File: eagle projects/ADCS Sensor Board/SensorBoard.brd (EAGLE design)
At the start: 91 x 91 mm, 85 parts, among them J5 HDR_10_EZFET_DEBUGGER, J6 MTI-1_8428-11B1-RK-TP, Q1 BC850SMD, Q2 IRF7507TRPBF, U1 MSP430F5529IPN, U2 LMV321, U3 ADS7841E_2K5, U4 LMV321, U5 LM20BIM7X_NOPB, U6 LMV321, Y1 32.768kHz, Y2 CSTCR4M00G15L99

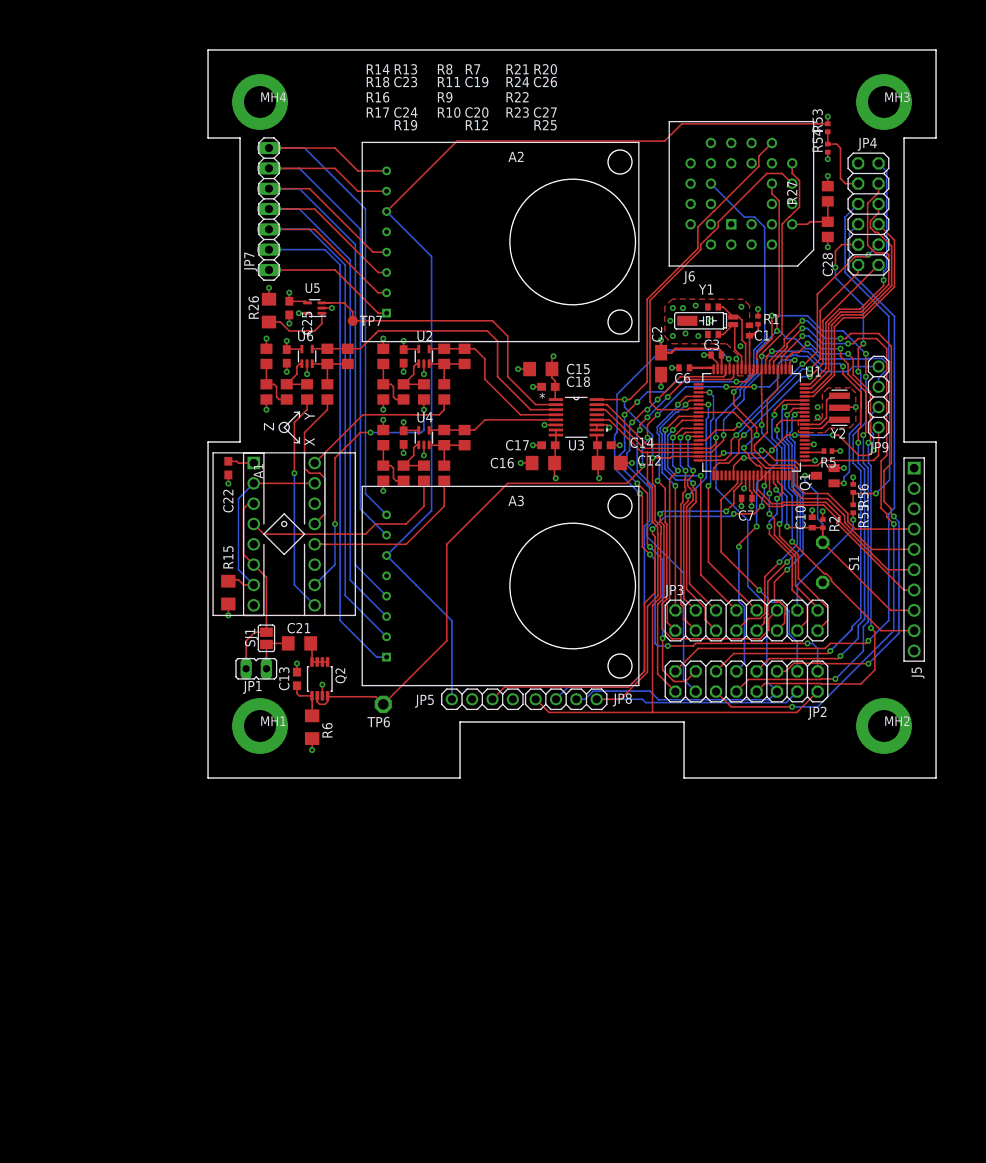
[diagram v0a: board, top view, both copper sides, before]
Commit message: Added copper pours to top and bottom. Fixed silksreens, smoothed traces
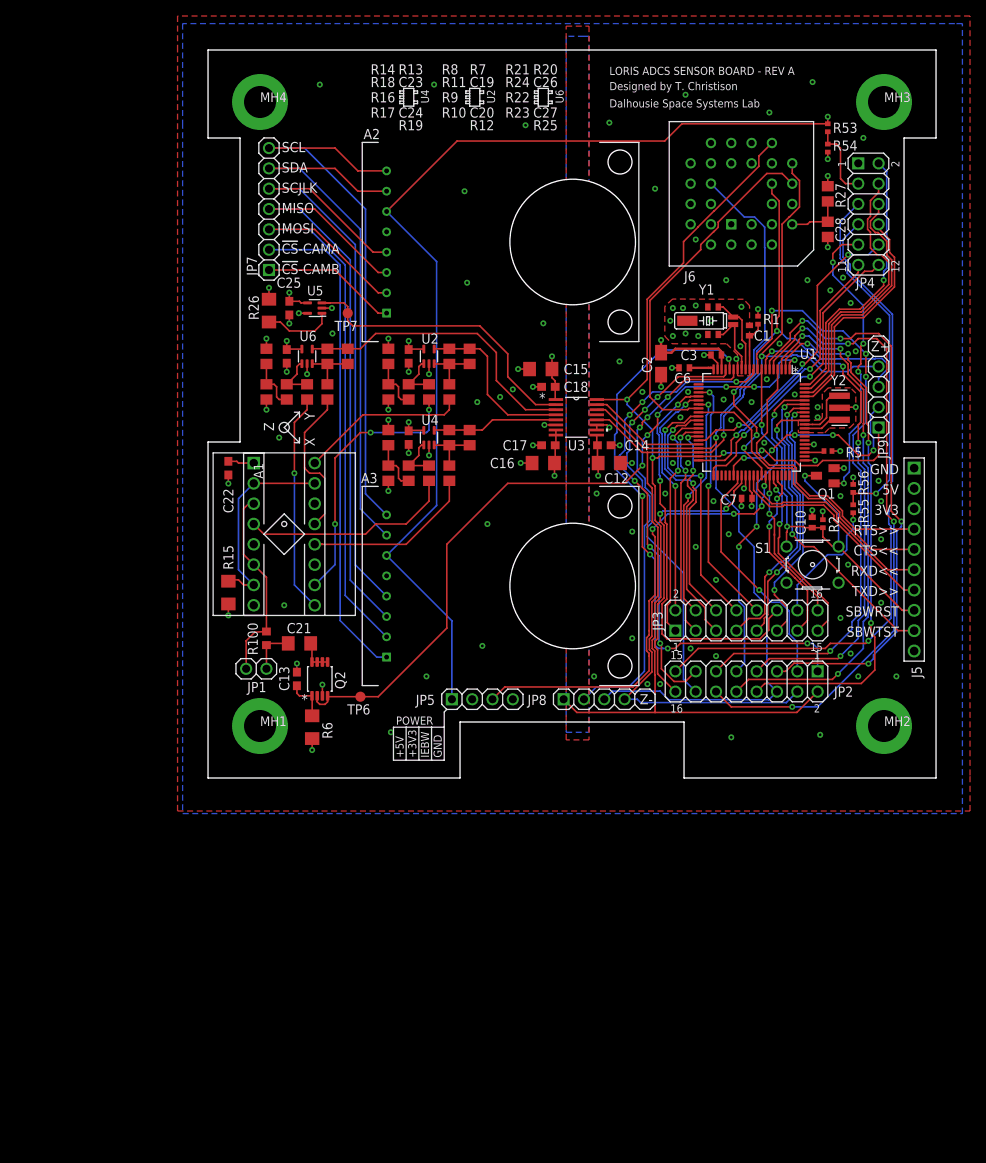
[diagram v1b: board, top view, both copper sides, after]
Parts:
- removed SJ1: (no value), jumper:SJ
- added R100: 0R, rcl:R0603
- JP1: device jumper:JP1 -> my_library:1X02
- JP2, JP3: device pinhead:2X08 -> my_library:2X08
- JP4: device pinhead:2X06 -> my_library:2X06
- JP7: device pinhead:1X07 -> my_library:1X07
- S1: device electricalmeter:PBTH -> my_library:B3F-10XX
- TP6: value TPPAD1-13 -> TPB1,27; device testpad:P1-13 -> testpad:B1,27
- moved JP8 3.49 mm to (48.3, 9.84)
- moved TP6 3.01 mm to (19.1, 10.2)
- moved S1 2.56 mm to (75.6, 26.7), turned to 0 degrees
- moved TP7 1.14 mm to (17.5, 58.1)
- moved C20 0.64 mm to (30.2, 52.7)
- moved C24 0.64 mm to (30.2, 42.5)
- moved R10 0.64 mm to (30.2, 48.3)
- moved R13 0.64 mm to (22.5, 42.5)
- moved R14 0.64 mm to (22.5, 38.1)
- moved R17 0.64 mm to (30.2, 38.1)
- moved R7 0.64 mm to (22.5, 52.7)
- moved R8 0.64 mm to (22.5, 48.3)
- moved C19 0.63 mm to (25.1, 52.7)
- moved C23 0.63 mm to (25.1, 42.5)
- moved R11 0.63 mm to (25.1, 48.3)
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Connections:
- net GND: now also S1.3, S1.4; no longer S1.1
- net N$35: now also R100.1; no longer SJ1.1
- net N$37: now also R100.2; no longer SJ1.2
- net RST/SBWTDIO: now also S1.1
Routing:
- net UCB0_SPI_MISO: track 135.0 -> 128.6 mm
- net UCB0_SPI_CLK: track 155.5 -> 151.8 mm
- net RST/SBWTDIO: track 51.8 -> 55.3 mm
- net !CS!_SUN_Z-: track 60.1 -> 56.6 mm
- net UCB0_SPI_MOSI: track 133.4 -> 129.9 mm
- net HMC1053_RESET: track 92.1 -> 90.2 mm
- net BRD_TEMP_MEAS: track 39.6 -> 38.2 mm
- net ACT_BRD_5V_PRESENT: track 15.1 -> 16.1 mm
- net MSP430_ACTIVE: track 36.8 -> 37.7 mm
- net !CS!_CURRENT_SENSE_1: track 76.4 -> 77.3 mm
- net +3V3: track 59.1 -> 58.3 mm
- net B_MEAS_Z: track 38.1 -> 37.2 mm
- net P1.7/CTS: track 37.8 -> 37.0 mm
- net P6.7/RTS: track 37.3 -> 36.6 mm
- net TEST/SBWTCK: track 39.1 -> 38.4 mm
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- added copper zone on layer 16, net GND
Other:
- board text added: "!CS!-CAMA"
- board text added: "!CS!-CAMB"
- board text added: "+3V3"
- board text added: "+5V"
- board text added: "IEBW"
- board text added: "MISO"
- board text added: "MOSI"
- board text added: "POWER"
- board text added: "SCJLK"
- board text added: "SCL"
- board text added: "SDA"
- board text added: "Z+"
- board text added: "Z-"
- board text removed: "RST"

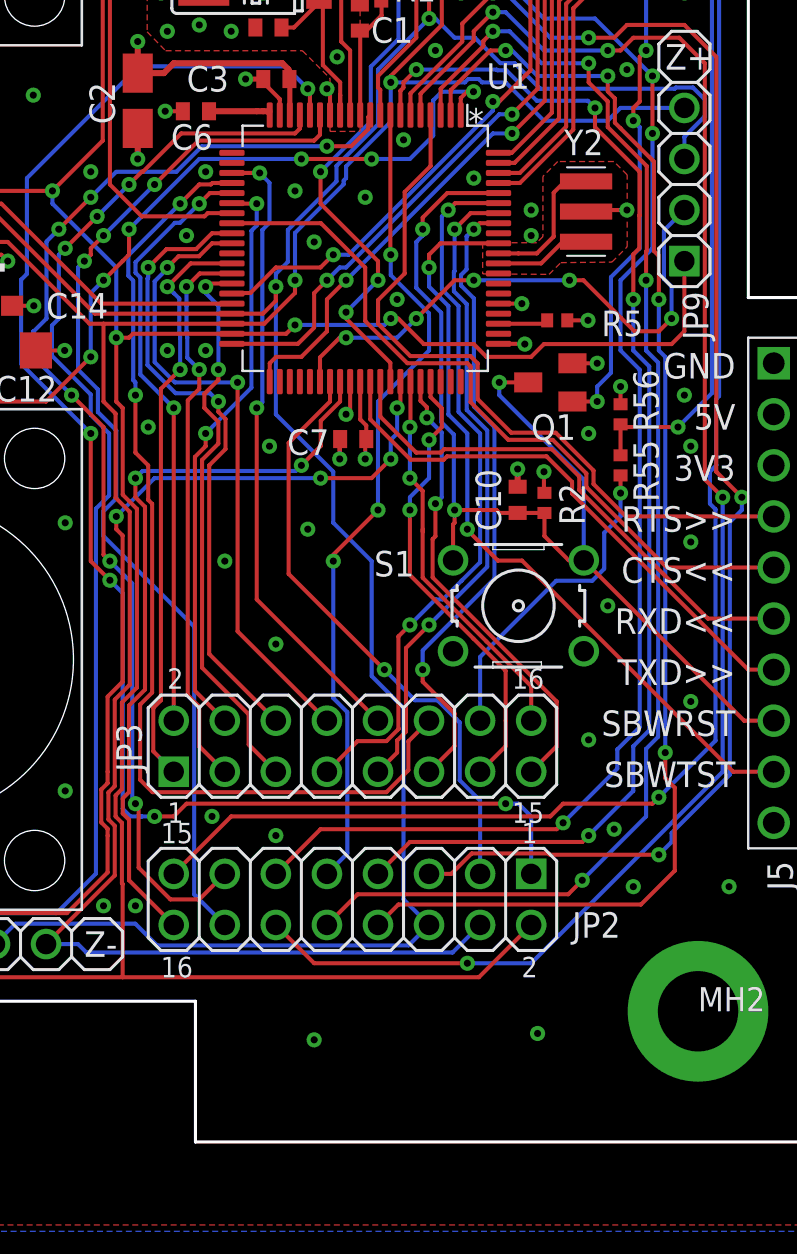
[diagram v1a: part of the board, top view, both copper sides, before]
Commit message: Added spi bus test headers
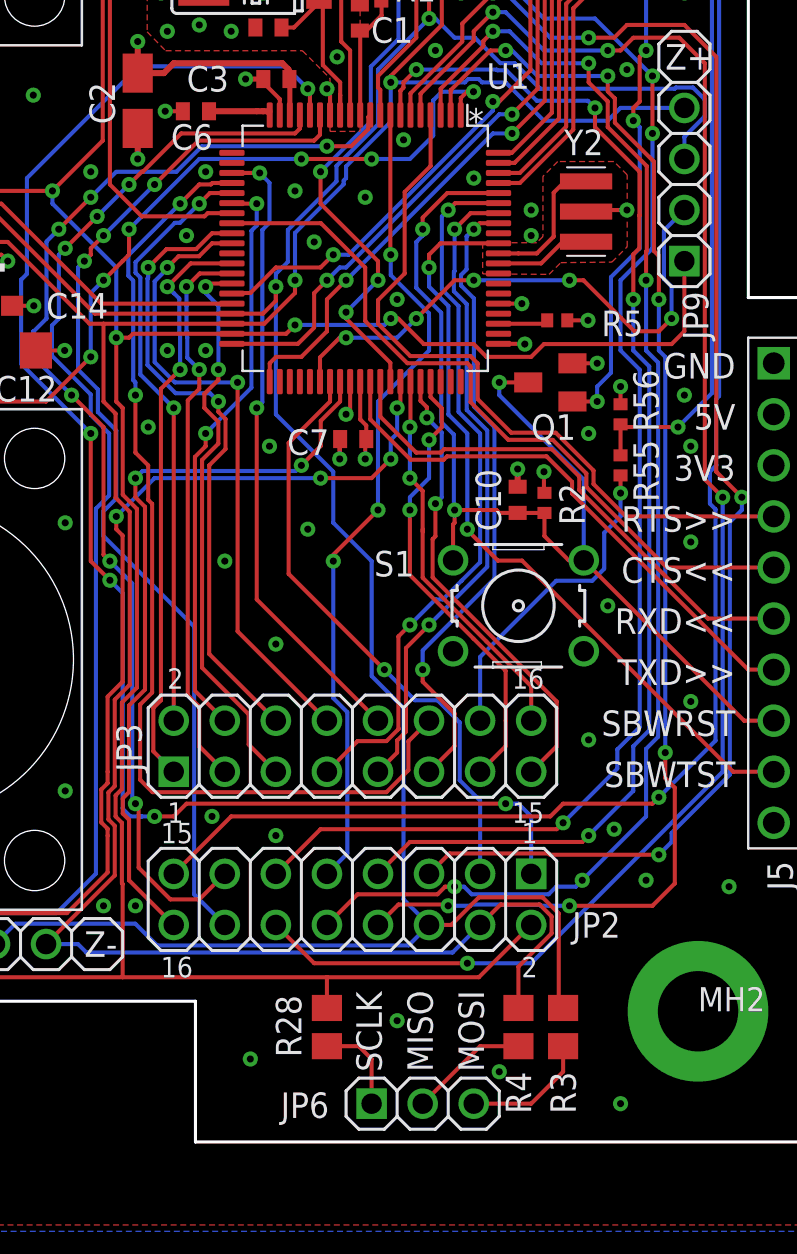
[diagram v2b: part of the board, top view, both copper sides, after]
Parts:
- added JP6: (no value), my_library:1X03
- added R28, R3, R4: 0R, rcl:R0805
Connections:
- new net N$1: JP6.1, R28.2
- new net N$2: JP6.2, R4.2
- new net N$3: JP6.3, R3.2
- net UCB0_SPI_CLK: now also R28.1
- net UCB0_SPI_MISO: now also R4.1
- net UCB0_SPI_MOSI: now also R3.1
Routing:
- net UCB0_SPI_MOSI: track 129.9 -> 142.0 mm
- net UCB0_SPI_MISO: track 128.6 -> 138.1 mm
- net N$3: track 0.00 -> 6.38 mm
- net N$2: track 0.00 -> 5.95 mm
- net N$1: track 0.00 -> 4.71 mm
- net UCB0_SPI_CLK: track 151.8 -> 153.3 mm
- net !CS!_SPEED_X: track 67.2 -> 67.7 mm, vias 4 -> 6
- net !CS!_SPEED_Y: track 67.9 -> 68.3 mm, vias 4 -> 5
- net GND: vias 121 -> 123
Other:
- board text added: "SCLK"

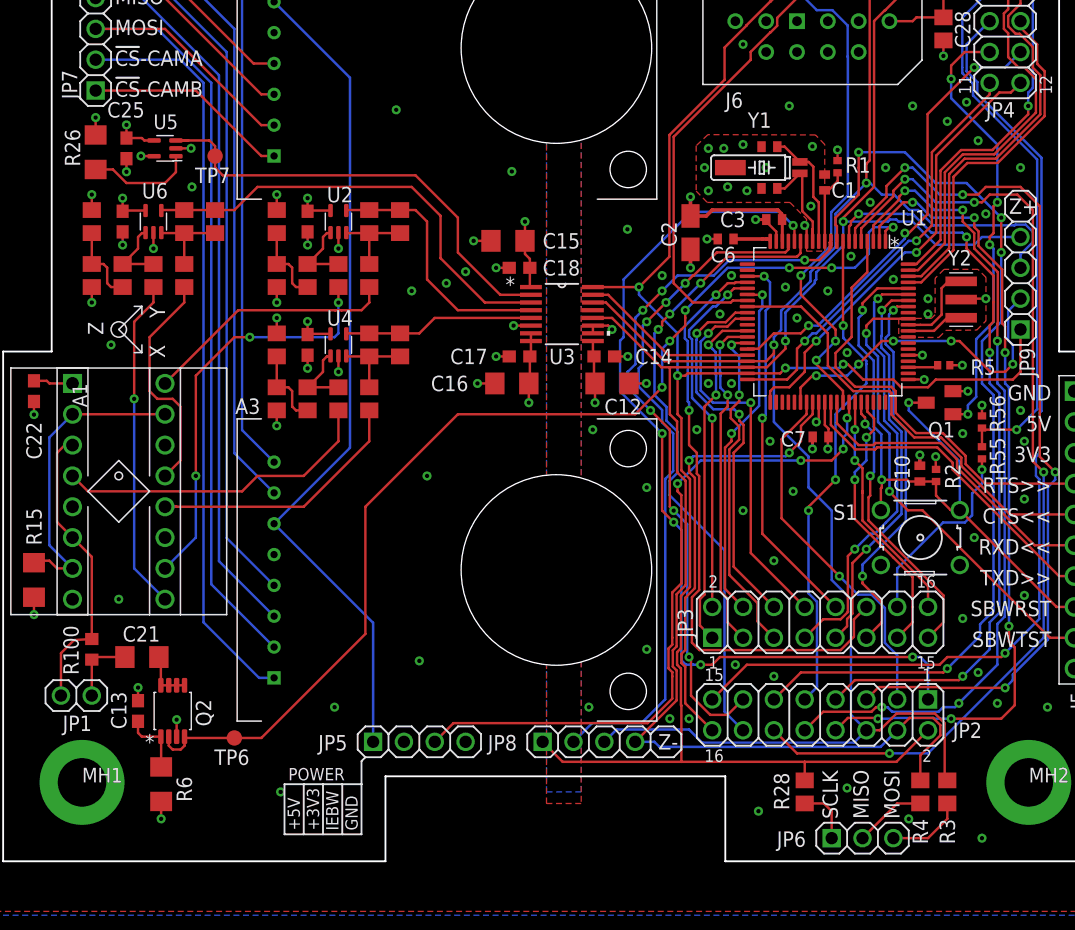
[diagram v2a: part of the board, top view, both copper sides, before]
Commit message: added indicator LEDs, drill legend, and adjusted board thickness
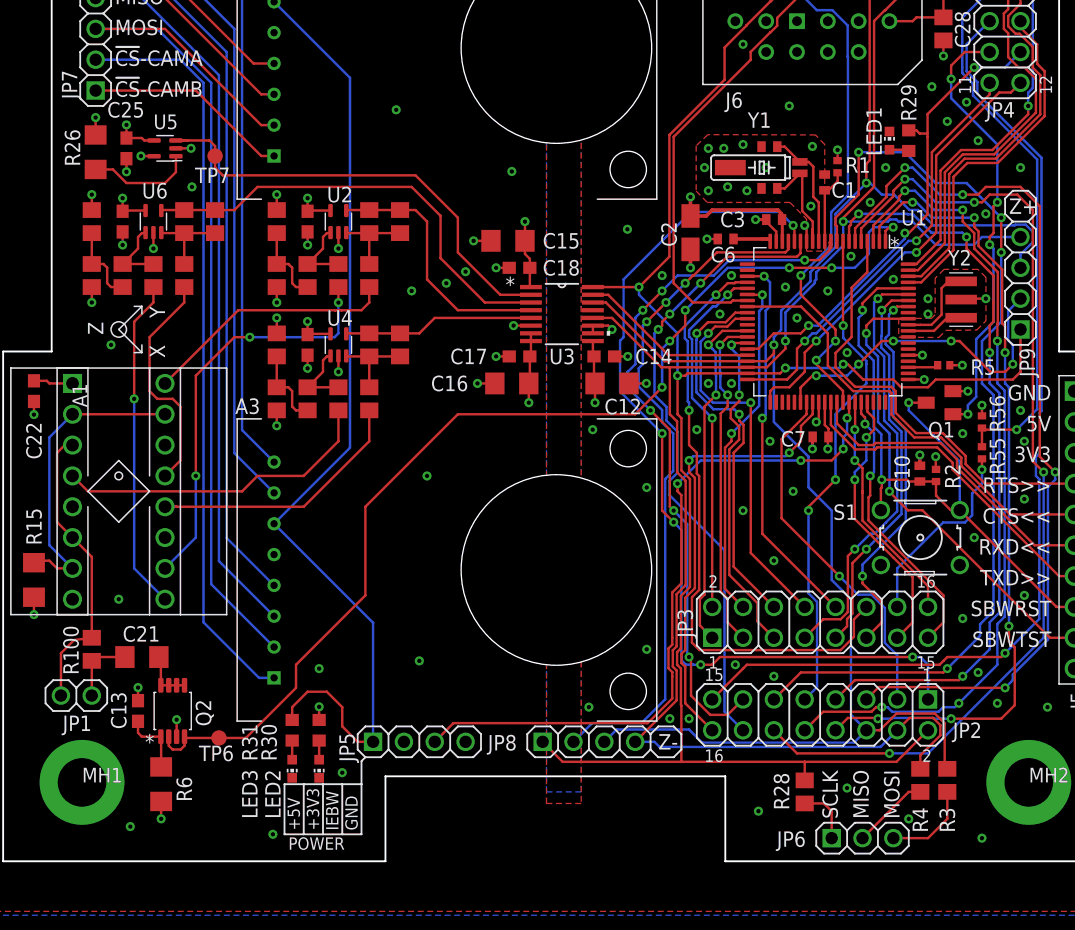
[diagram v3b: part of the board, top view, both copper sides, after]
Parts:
- added DRILEGEND: (no value), drilegend:DRILEGEND
- added LED1, LED2, LED3: (no value), led:CHIP-LED0603
- added R29, R30: 470R, rcl:R0603
- added R31: 750R, rcl:R0603
- R100: device rcl:R0603 -> rcl:R0805
- moved TP6 1.27 mm to (17.8, 10.2)
- moved R3 0.95 mm to (77.8, 6.67)
- moved R4 0.95 mm to (75.6, 6.67)
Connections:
- new net N$4: LED1.A, R29.2
- new net N$5: LED2.A, R30.2
- new net N$6: LED3.A, R31.2
- net +3V3: now also R30.1
- net +5V: now also R31.1
- net GND: now also LED1.C, LED2.C, LED3.C
- net MSP430_ACTIVE: now also R29.1
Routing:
- net +5V: track 130.1 -> 141.0 mm
- net MSP430_ACTIVE: track 37.7 -> 39.4 mm
- net N$4: track 0.00 -> 1.63 mm
- net N$6: track 0.00 -> 1.58 mm
- net N$5: track 0.00 -> 1.58 mm
- net +3V3: track 58.3 -> 59.4 mm, vias 16 -> 17
- net UCB0_SPI_MOSI: track 142.0 -> 141.1 mm
- net N$3: track 6.38 -> 7.33 mm
- net UCB0_SPI_MISO: track 138.1 -> 137.1 mm
- net HMC1053_RESET: track 90.2 -> 89.5 mm
- net GND: vias 123 -> 125
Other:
- board text added: "01-16"
- board text added: "01-20"
- board text added: "LAYER-STACK"

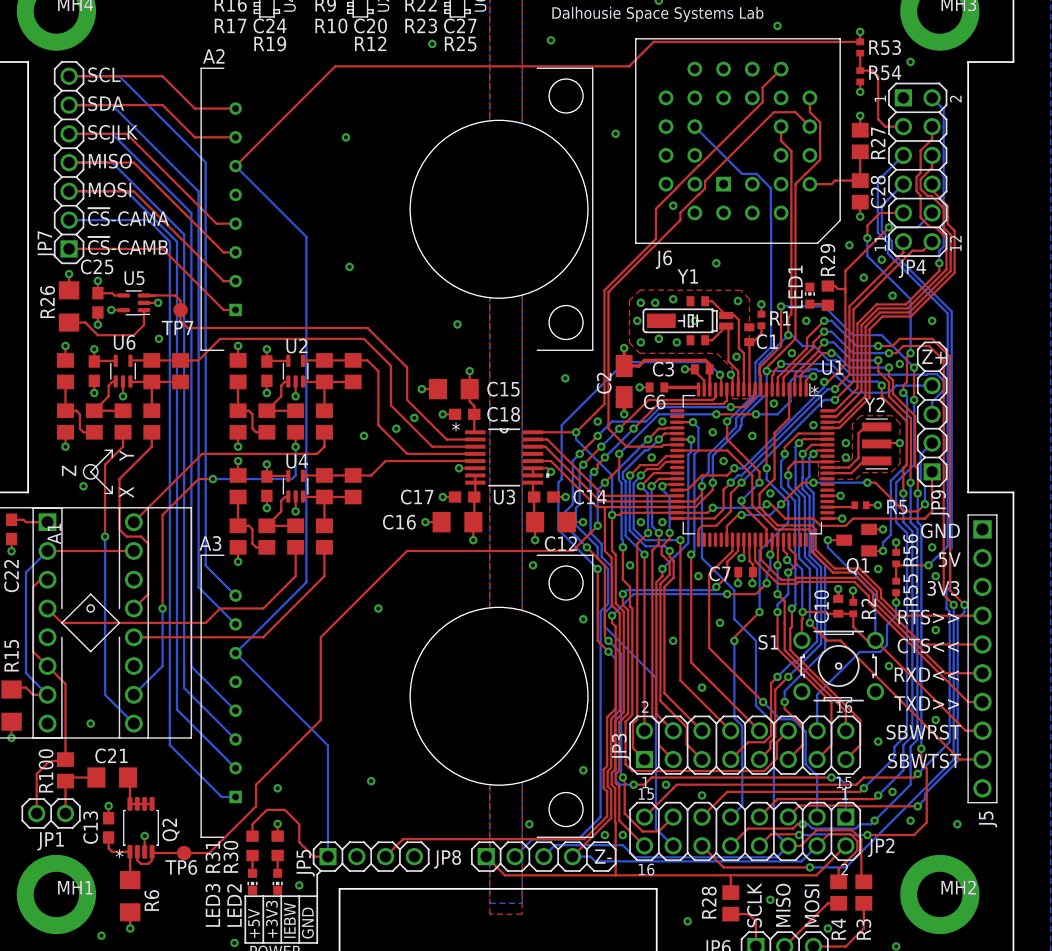
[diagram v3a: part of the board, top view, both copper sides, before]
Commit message: Updated traces/ vias to meet manufacturer DRC
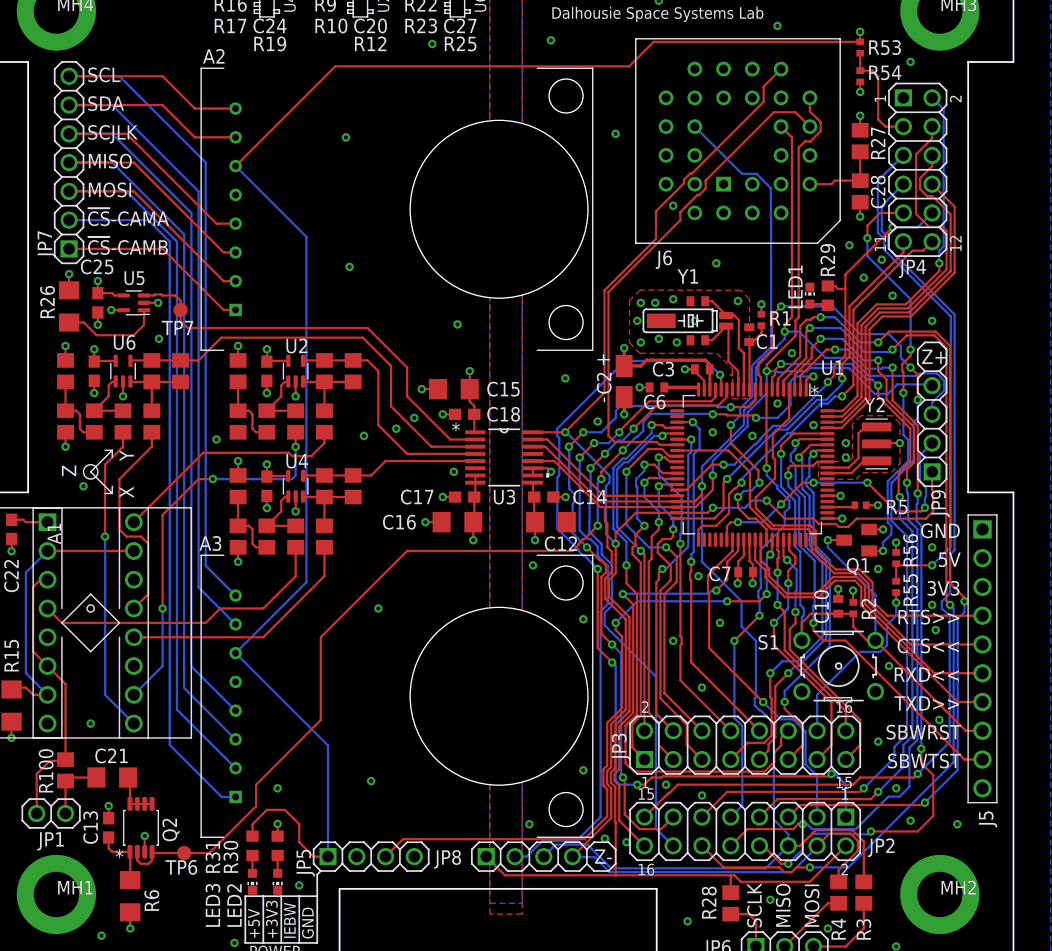
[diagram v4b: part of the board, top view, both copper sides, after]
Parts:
- C2: device rcl:A/3216-18R -> my_library:A/3216-18R
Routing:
- net GND: track 53.9 -> 48.8 mm, vias 125 -> 112
- net UCB0_SPI_CLK: track 153.3 -> 156.8 mm
- net !CS!_SPEED_Z: track 81.3 -> 84.5 mm
- net RST/SBWTDIO: track 55.3 -> 58.4 mm, vias 3 -> 2
- net MAG_Y_RIN: track 31.9 -> 28.8 mm
- net !CS!_SPEED_X: track 67.7 -> 70.6 mm
- net UCB0_SPI_MISO: track 137.1 -> 139.7 mm
- net !COUNT_EN: track 74.5 -> 76.7 mm
- net RW_X_SPEED_CTRL: track 29.1 -> 31.2 mm
- net P4.5/UCA1RXD: track 26.0 -> 28.1 mm
- net UCB0_SPI_MOSI: track 141.1 -> 143.1 mm
- net P4.4/UCA1TXD: track 27.6 -> 29.6 mm
- net MAG_X_RIN: track 50.4 -> 52.1 mm
- net !CS!_CURRENT_SENSE_2: track 58.1 -> 59.8 mm
- net RW_X_DIR: track 35.7 -> 37.4 mm
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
